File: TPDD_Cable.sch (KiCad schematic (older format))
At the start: 5 parts, among them J1 Wire Solder Pads, J2 TPDD, Q1 DTA114EKA, Q2 DTA114EKA, Q3 DTA114EKA

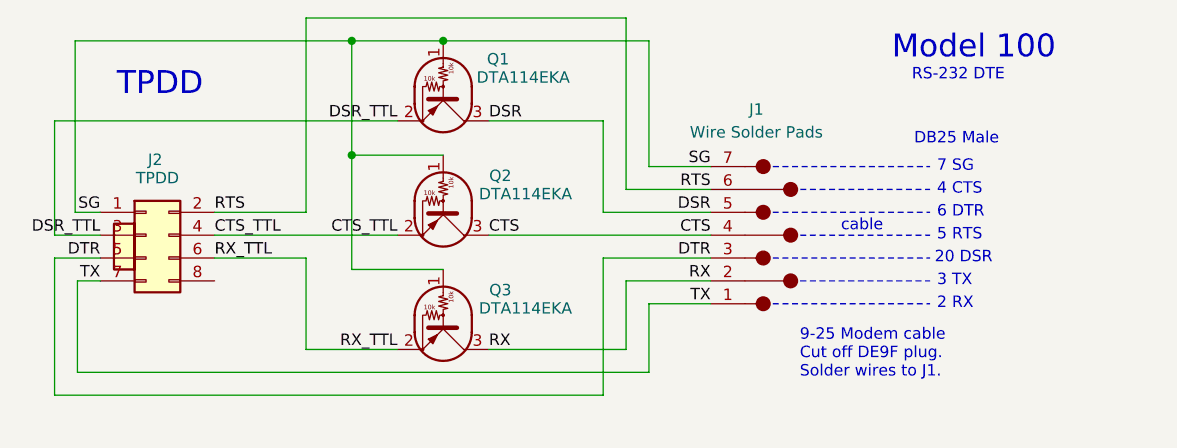
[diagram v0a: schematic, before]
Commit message: add schematic svg for readme
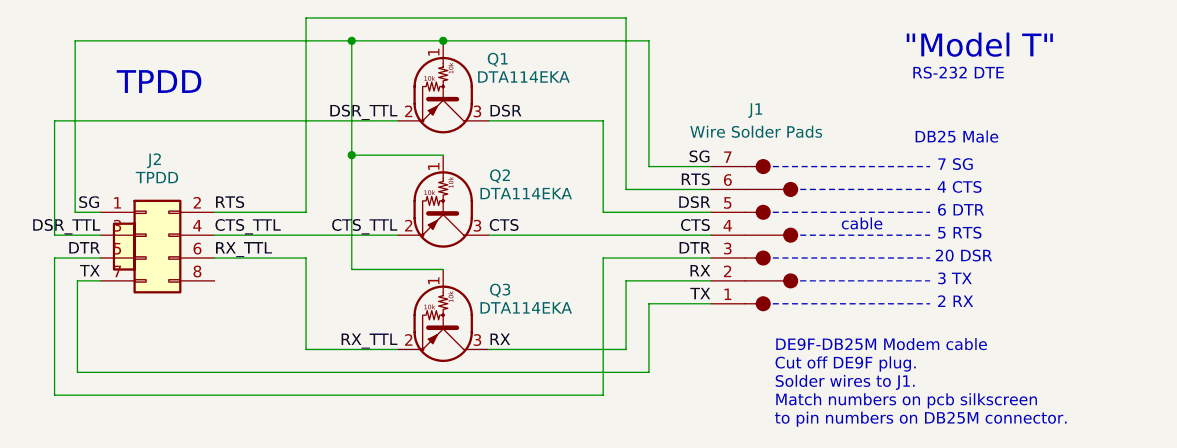
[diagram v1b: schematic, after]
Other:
- note added: ""Model T""
- note added: "DE9F-DB25M Modem cable\nCut off DE9F plug.\nSolder wires to J1.\nMatch numbers on pcb silkscreen\nto pin numbers on DB25M connector."
- note removed: "9-25 Modem cable\nCut off DE9F plug.\nSolder wires to J1."
- note removed: "Model 100"
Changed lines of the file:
@@
 	4700 4050 5100 4050
 Text Notes 7780 3140 2    100  ~ 0
-Model 100
+"Model T"
 Text Notes 4050 3300 2    100  ~ 0
 TPDD
@@
 Wire Wire Line
 	3490 3050 3490 3800
-Text Notes 6660 4530 0    50   ~ 0
-9-25 Modem cable\nCut off DE9F plug.\nSolder wires to J1.
+Text Notes 6550 4740 0    50   ~ 0
+DE9F-DB25M Modem cable\nCut off DE9F plug.\nSolder wires to J1.\nMatch numbers on pcb silkscreen\nto pin numbers on DB25M connector.
 Wire Wire Line
 	4500 3800 4100 3800
